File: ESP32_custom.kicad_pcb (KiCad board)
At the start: 4 copper layers, 32 x 42.2 mm, 28 parts, among them J1 TYPE-C-31-M-12, J2 Conn_01x16_Pin, J3 Conn_01x16_Pin, Q1 SS8050, Q2 SS8050, SW1 SW_Push, SW2 SW_Push, U2 ESP32-WROOM-32E 8MB, U3 CH340C, U4 AMS1117-3.3

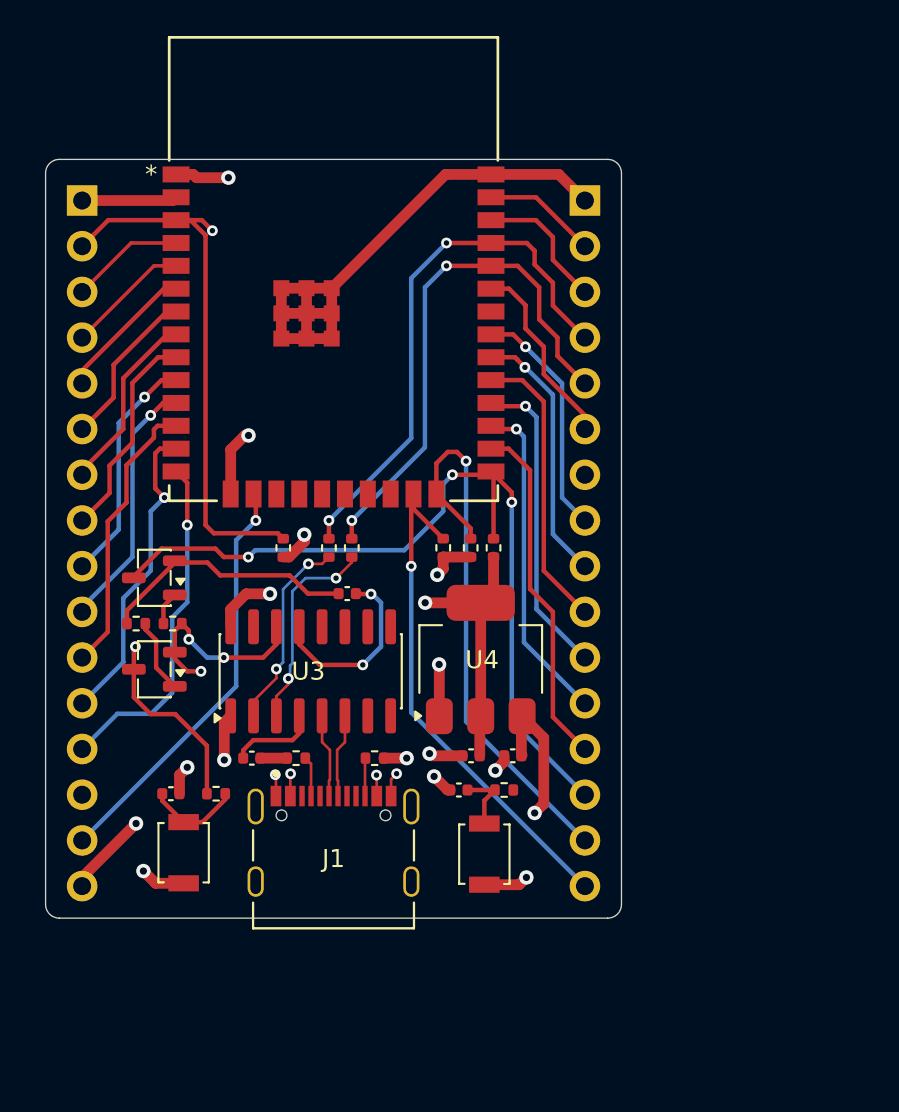
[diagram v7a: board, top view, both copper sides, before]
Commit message: update schematic (reduced pin header)
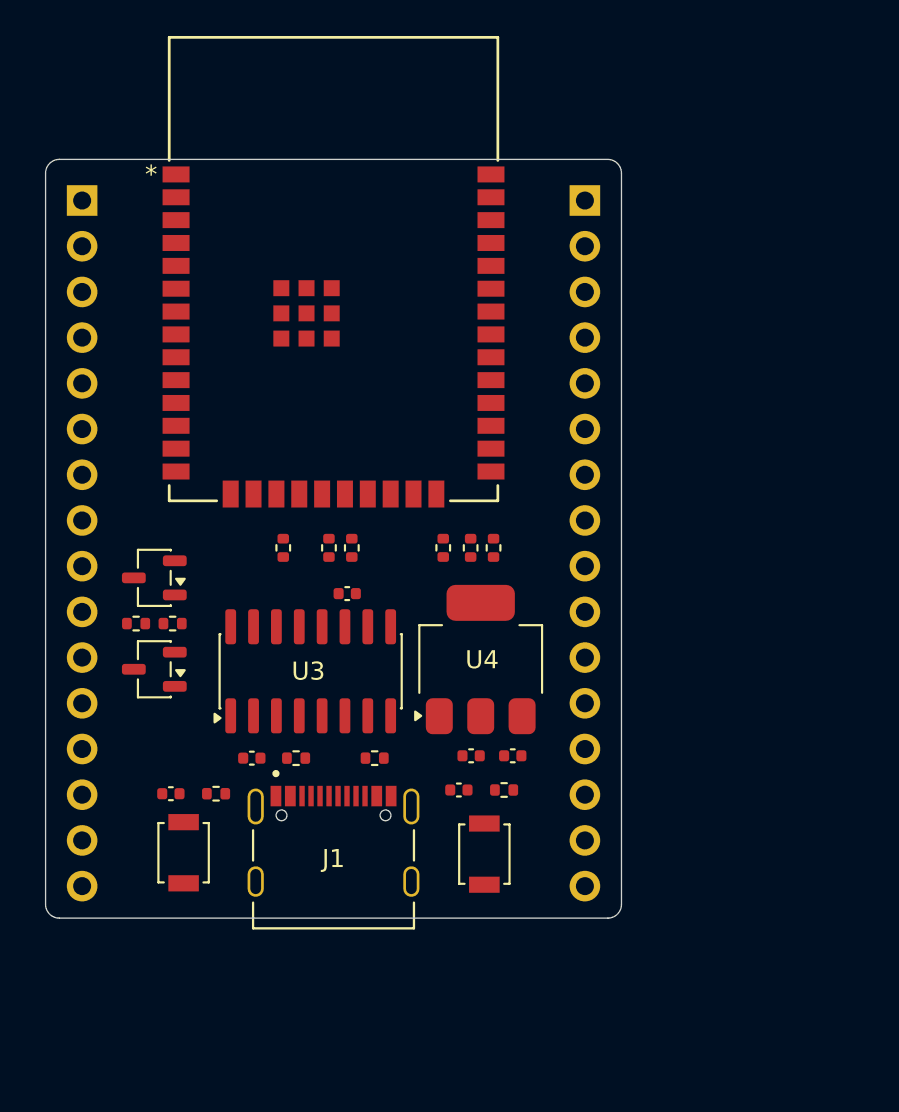
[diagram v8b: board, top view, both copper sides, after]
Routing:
- net /EN: track 66.4 -> 0.00 mm, vias 2 -> 0
- net GND: track 65.1 -> 0.00 mm, vias 14 -> 0
- net /IO0: track 47.5 -> 0.00 mm, vias 3 -> 0
- net /IO2: track 30.9 -> 0.00 mm, vias 1 -> 0
- net /RX: track 30.2 -> 0.00 mm, vias 2 -> 0
- net /TX: track 29.4 -> 0.00 mm, vias 2 -> 0
- net /IO15: track 29.0 -> 0.00 mm, vias 1 -> 0
- net VCC: track 25.2 -> 0.00 mm, vias 3 -> 0
- net /IO13: track 23.3 -> 0.00 mm, vias 1 -> 0
- net /IO4: track 19.4 -> 0.00 mm
- net /IO12: track 19.2 -> 0.00 mm, vias 1 -> 0
- net /IO16: track 18.3 -> 0.00 mm, vias 1 -> 0
- net /IO17: track 17.3 -> 0.00 mm, vias 1 -> 0
- net /IO14: track 17.3 -> 0.00 mm, vias 1 -> 0
- net /IO5: track 16.1 -> 0.00 mm
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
